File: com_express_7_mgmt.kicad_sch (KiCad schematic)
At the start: 79 parts, among them J12 Plug_Bus_CE7_EPT_401-51501-51, J13 PinHeader_1x3_P2.54mm_Drill1.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, J14 PinHeader_1x3_P2.54mm_Drill1.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, Q11 BSS138-7-F, Q12 BSS138-7-F, SW1 SW_1-1825027-1_THT, SW2 SW_1-1825027-1_THT, U30 74AUP2G132, U31 M24C64-F_DFN8, U32 TPS3840PL30DBVR, U33 74AUP2G132, U34 MAX16150A_SOT, U35 74AUP2G132, U36 W25Q32FV_SOIC-8

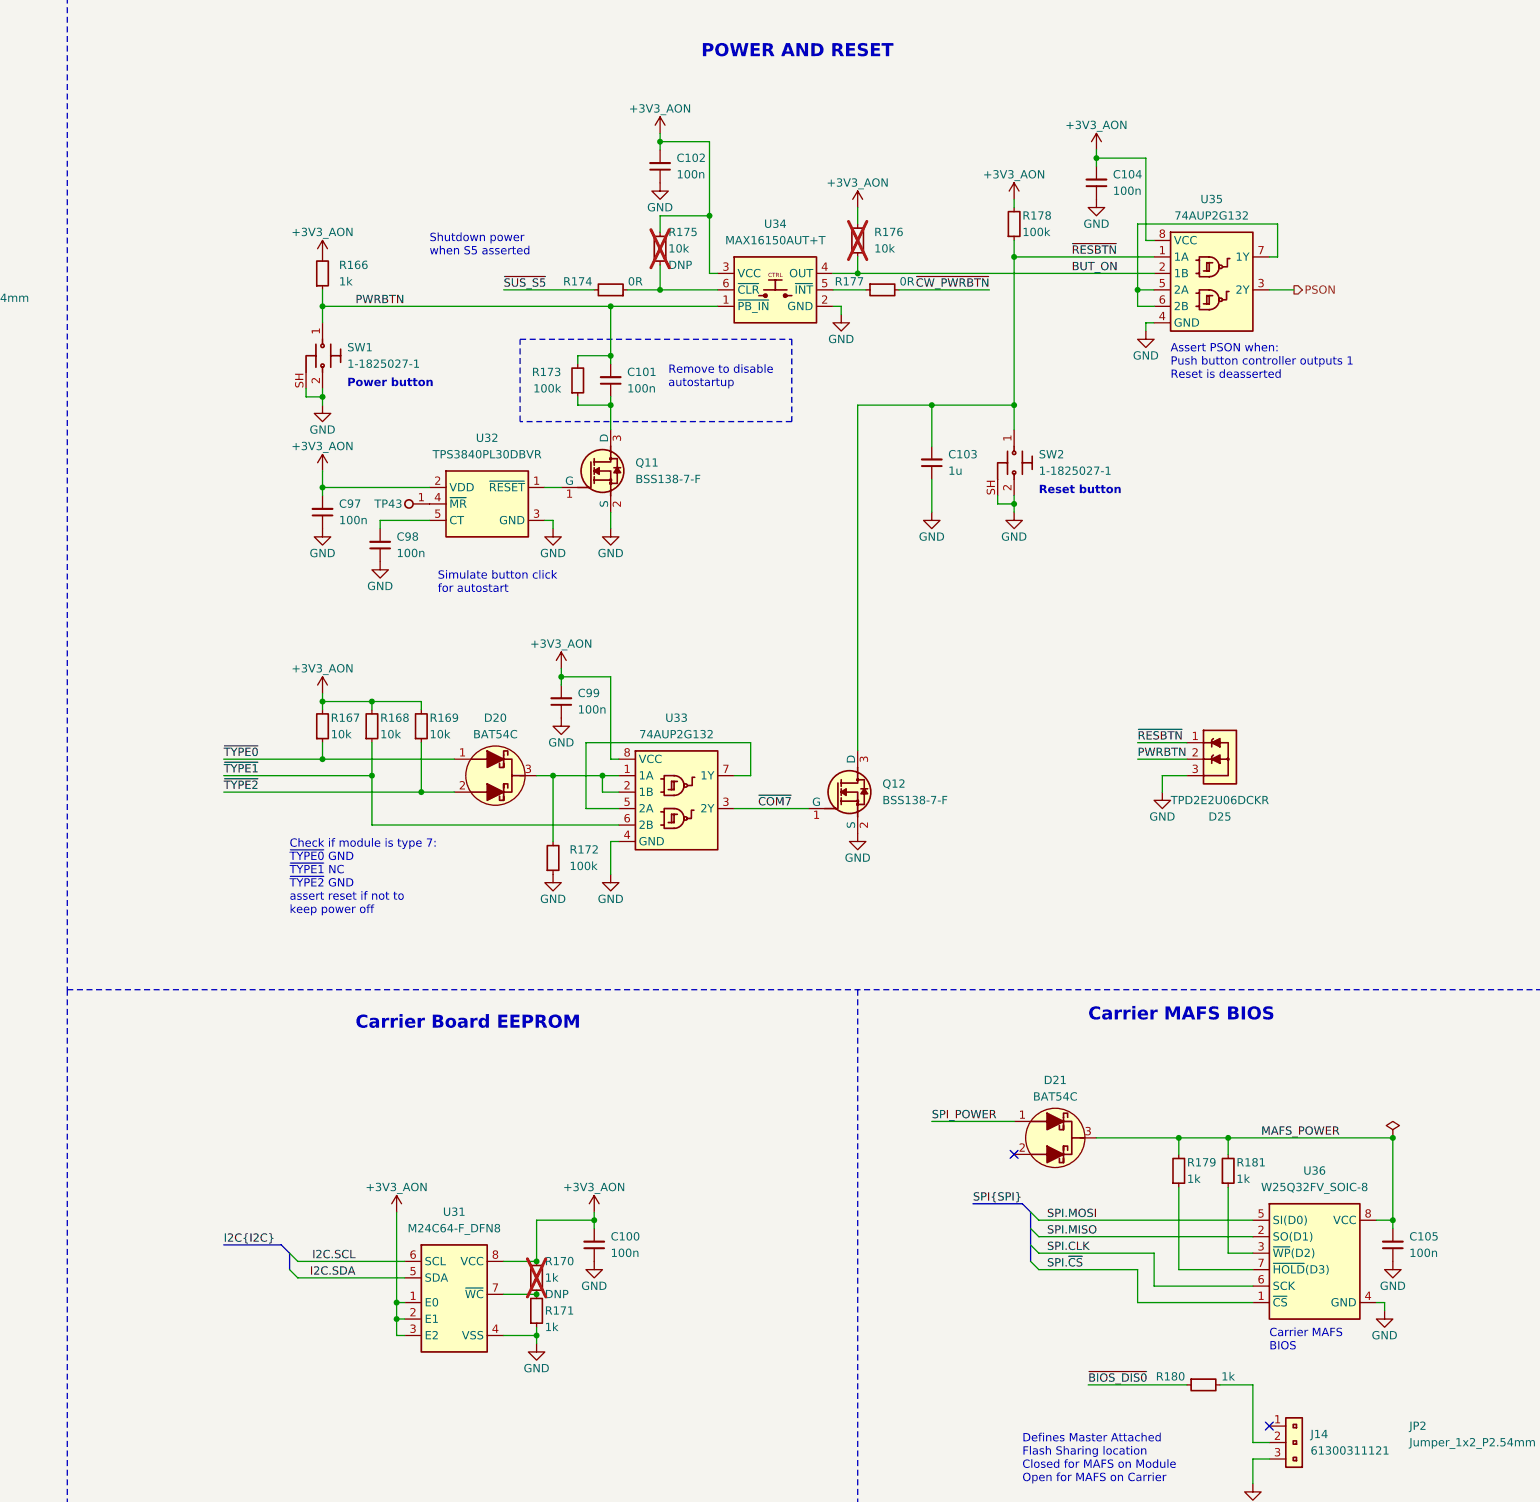
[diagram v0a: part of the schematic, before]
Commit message: [#58904] Remove 0R on MicroSD
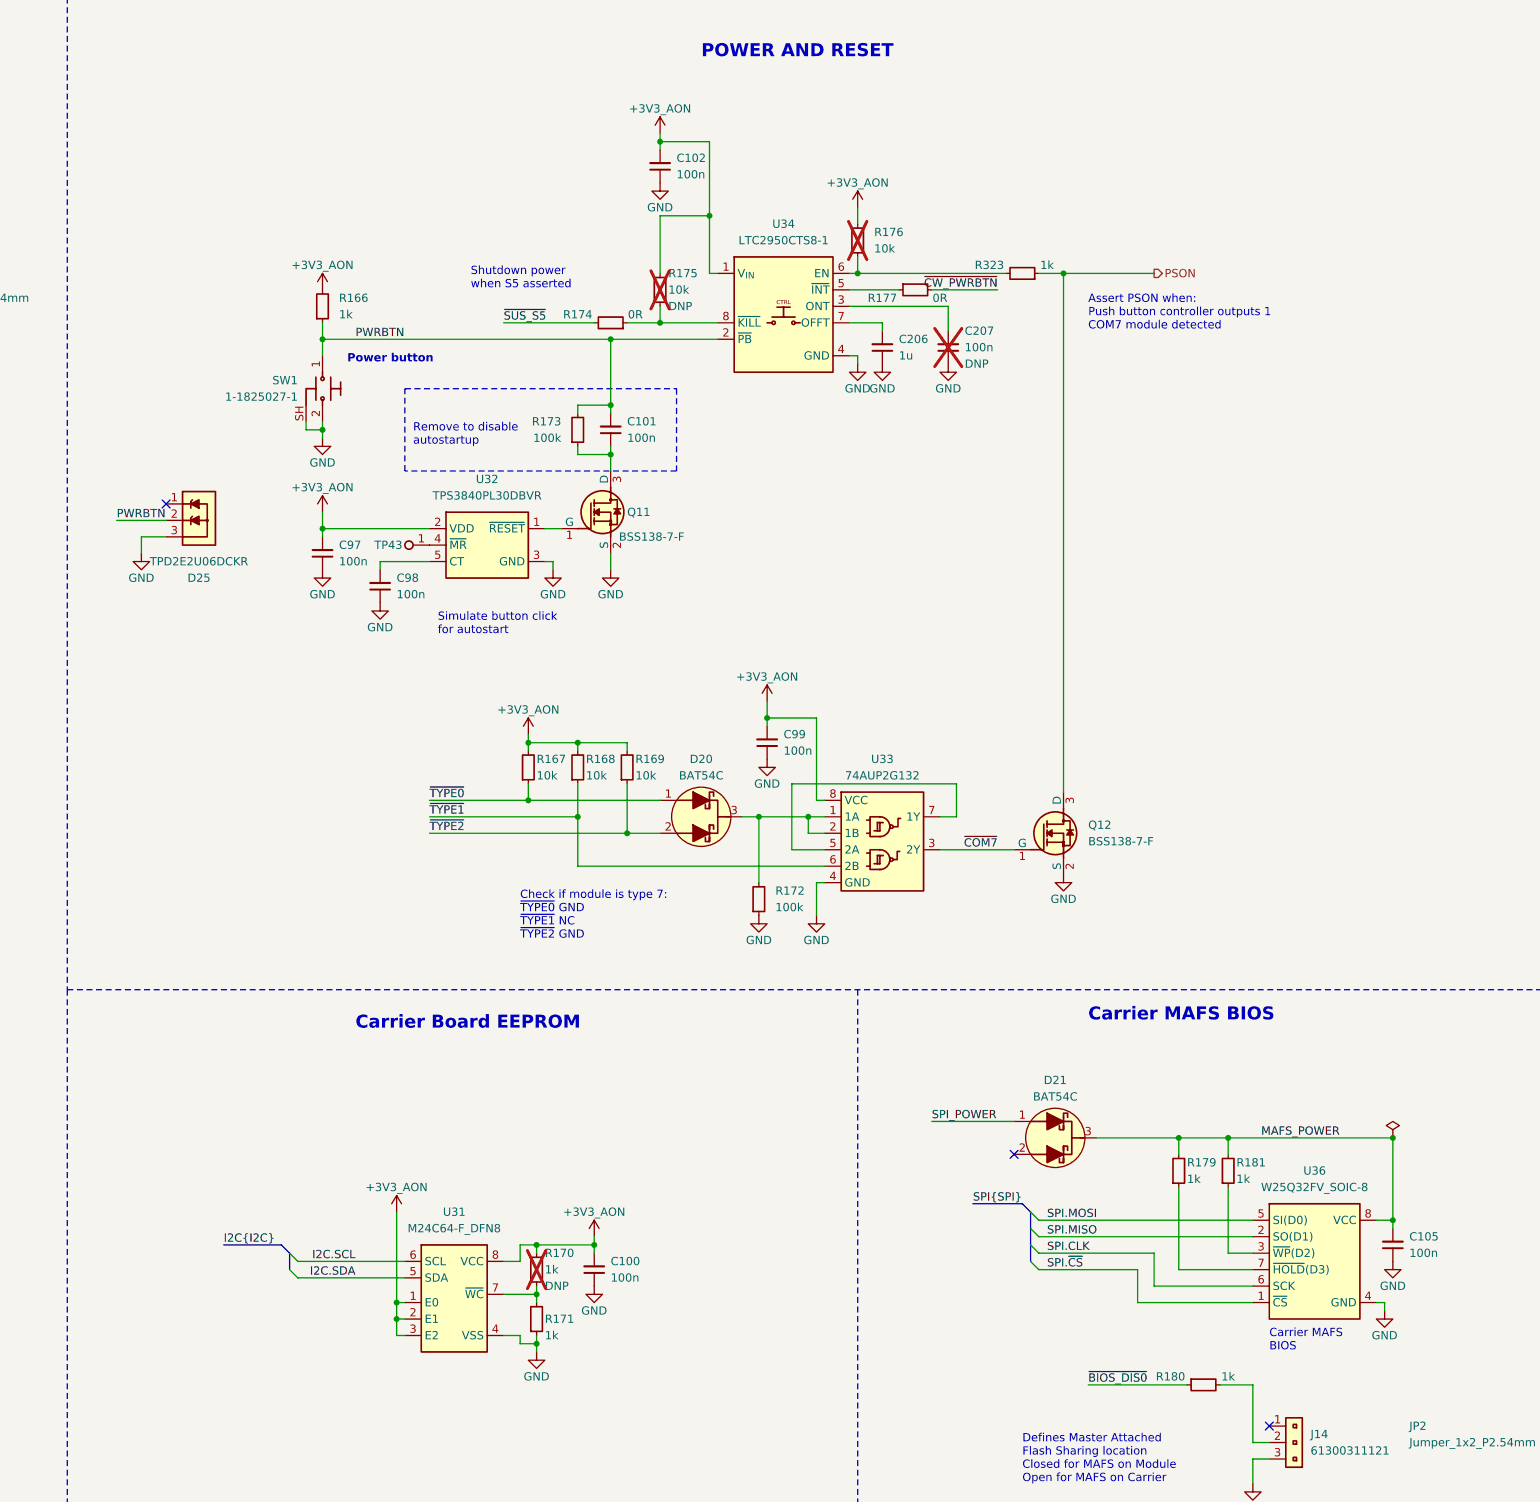
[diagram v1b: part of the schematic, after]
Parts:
- removed C103: C_1u_0402, antmicro-footprints:C_0402_1005Metric, symbol antmicroCapacitors0402:C_1u_0402
- removed C104: C_100n_0402, antmicro-footprints:C_0402_1005Metric, symbol antmicroCapacitors0402:C_100n_0402
- removed R178: R_100k_0402, antmicro-footprints:R_0402_1005Metric, symbol antmicroResistors0402:R_100k_0402
- removed SW2: SW_1-1825027-1_THT, antmicro-footprints:SW_1-1825027-1_THT, symbol antmicroPushbuttonSwitches:SW_1-1825027-1_THT
- removed U34: MAX16150A_SOT, antmicro-footprints:SOT-23-6, symbol antmicroPMICPowerSequencers:MAX16150A_SOT
- removed U35: 74AUP2G132, antmicro-footprints:VSSOP-8_2.3x2mm_P0.5mm, symbol antmicroLogicGatesandInverters:74AUP2G132
- added C206: C_1u_0402, antmicro-footprints:C_0402_1005Metric, symbol antmicroCapacitors0402:C_1u_0402
- added C207: C_100n_0402, antmicro-footprints:C_0402_1005Metric, symbol antmicroCapacitors0402:C_100n_0402
- added R323: R_1k_0402, antmicro-footprints:R_0402_1005Metric, symbol antmicroResistors0402:R_1k_0402
- added U34: LTC2950CTS8-1, antmicro-footprints:SOT-23-8, symbol antmicroPMICPowerSequencers:LTC2950CTS8-1
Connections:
- net +3V3_AON: now also U34.1 (V_{IN})
- net GND: now also C206.1, C207.1, U34.4 (GND)
- net PSON: now also Q12.3 (D), R323.1
- net PWRBTN: now also U34.2 (~{PB})
- net at R174.1, R175.1: now also U34.8 (~{KILL})
- net at R177.1: now also U34.5 (~{INT})
- net BUT_ON: no longer names the net of R176.1
- net BUT_ON: now also R323.2, U34.6 (EN)
- net ~{RESBTN}: no longer names the net of D25.1
- net ~{RESBTN}: no longer Q12.3 (D)
- new net: C206.2, U34.7 (OFFT)
- new net: C207.2, U34.3 (ONT)
- no-connect marks 6 -> 7
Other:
- note added: "Assert PSON when: Push button controller outputs 1 COM7 module detected"
- note added: "Check if module is type 7: ~{TYPE0} GND ~{TYPE1} NC ~{TYPE2} GND"
- note removed: "Assert PSON when: Push button controller outputs 1 Reset is deasserted"
- note removed: "Check if module is type 7: ~{TYPE0} GND ~{TYPE1} NC ~{TYPE2} GND assert reset if not to keep power off"
- note removed: "Reset button"
- moved on the sheet: C100, C101, C97, C98, C99, D20, D25, Q11, Q12, R166, R167, R168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

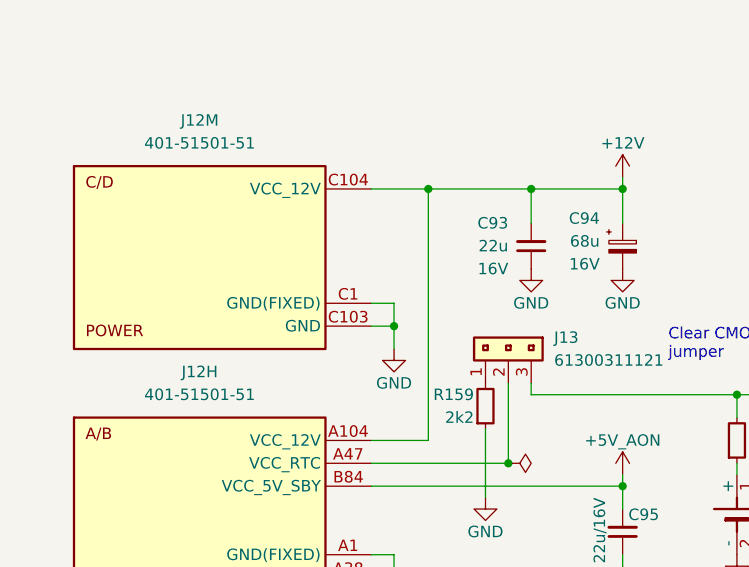
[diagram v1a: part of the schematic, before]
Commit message: [#58904] Fix DRC
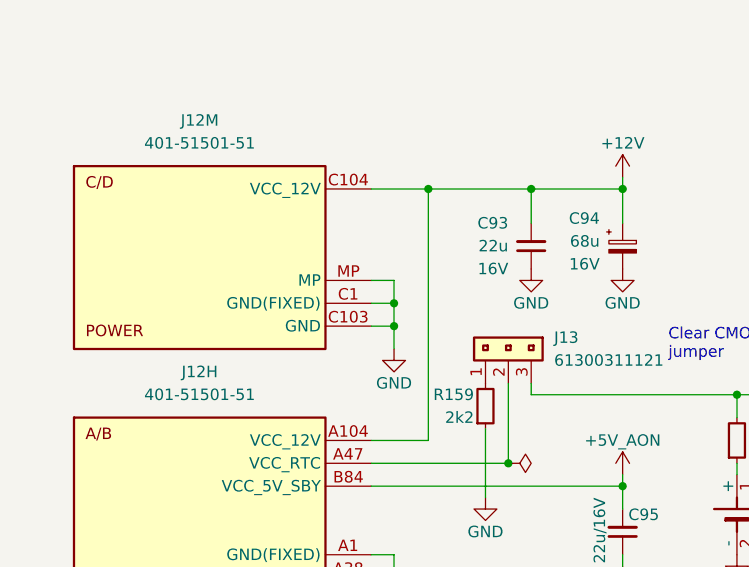
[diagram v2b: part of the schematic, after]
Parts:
- J12: Manufacturer EPT -> ept
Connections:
- net GND: now also J12.MP
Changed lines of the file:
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@@
   (junction (at 248.92 140.97) (diameter 0) (color 0 0 0 0)
   )
+  (junction (at 78.74 50.8) (diameter 0) (color 0 0 0 0)
+  )
   (junction (at 259.08 209.55) (diameter 0) (color 0 0 0 0)
   )
@@
     (stroke (width 0) (type default))
   )
+  (wire (pts (xy 76.2 48.26) (xy 78.74 48.26))
+    (stroke (width 0) (type default))
+  )
   (wire (pts (xy 229.87 223.52) (xy 228.6 223.52))
     (stroke (width 0) (type default))
@@
     (stroke (width 0) (type default))
   )
+  (wire (pts (xy 78.74 48.26) (xy 78.74 50.8))
+    (stroke (width 0) (type default))
+  )
   (wire (pts (xy 327.66 208.28) (xy 360.68 208.28))
     (stroke (width 0) (type default))
@@
       (effects (font (size 1.27 1.27) (thickness 0.15)) (justify left bottom) hide)
     )
-    (property "Manufacturer" "EPT" (at 129.54 243.84 0)
+    (property "Manufacturer" "ept" (at 129.54 243.84 0)
       (effects (font (size 1.27 1.27) (thickness 0.15)) (justify left bottom) hide)
     )
@@
     (pin "A80")
     (pin "B18")
+    (pin "MP")
     (instances
       (project "com-express-7-baseboard"
@@
       (effects (font (size 1.27 1.27) (thickness 0.15)) (justify left bottom) hide)
     )
-    (property "Manufacturer" "EPT" (at 129.54 43.18 0)
+    (property "Manufacturer" "ept" (at 129.54 43.18 0)
       (effects (font (size 1.27 1.27) (thickness 0.15)) (justify left bottom) hide)
     )
@@
     (pin "A80")
     (pin "B18")
+    (pin "MP")
     (instances
       (project "com-express-7-baseboard"
@@
       (effects (font (size 1.27 1.27) (thickness 0.15)) (justify left bottom) hide)
     )
-    (property "Manufacturer" "EPT" (at 129.54 71.12 0)
+    (property "Manufacturer" "ept" (at 129.54 71.12 0)
       (effects (font (size 1.27 1.27) (thickness 0.15)) (justify left bottom) hide)
     )
@@
     (pin "A80")
     (pin "B18")
+    (pin "MP")
     (instances
       (project "com-express-7-baseboard"
@@
       (effects (font (size 1.27 1.27) (thickness 0.15)) (justify left bottom) hide)
     )
-    (property "Manufacturer" "EPT" (at 129.54 218.44 0)
+    (property "Manufacturer" "ept" (at 129.54 218.44 0)
       (effects (font (size 1.27 1.27) (thickness 0.15)) (justify left bottom) hide)
     )
@@
     (pin "A80")
     (pin "B18")
+    (pin "MP")
     (instances
       (project "com-express-7-baseboard"
@@
       (effects (font (size 1.27 1.27) (thickness 0.15)) (justify left bottom) hide)
     )
-    (property "Manufacturer" "EPT" (at 129.54 111.76 0)
+    (property "Manufacturer" "ept" (at 129.54 111.76 0)
       (effects (font (size 1.27 1.27) (thickness 0.15)) (justify left bottom) hide)
     )
@@
     (pin "A80")
     (pin "B18")
+    (pin "MP")
     (instances
       (project "com-express-7-baseboard"
